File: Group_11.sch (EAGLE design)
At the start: 28 parts, among them J1 POWER_JACKPTH_LOCK, U1 +12v

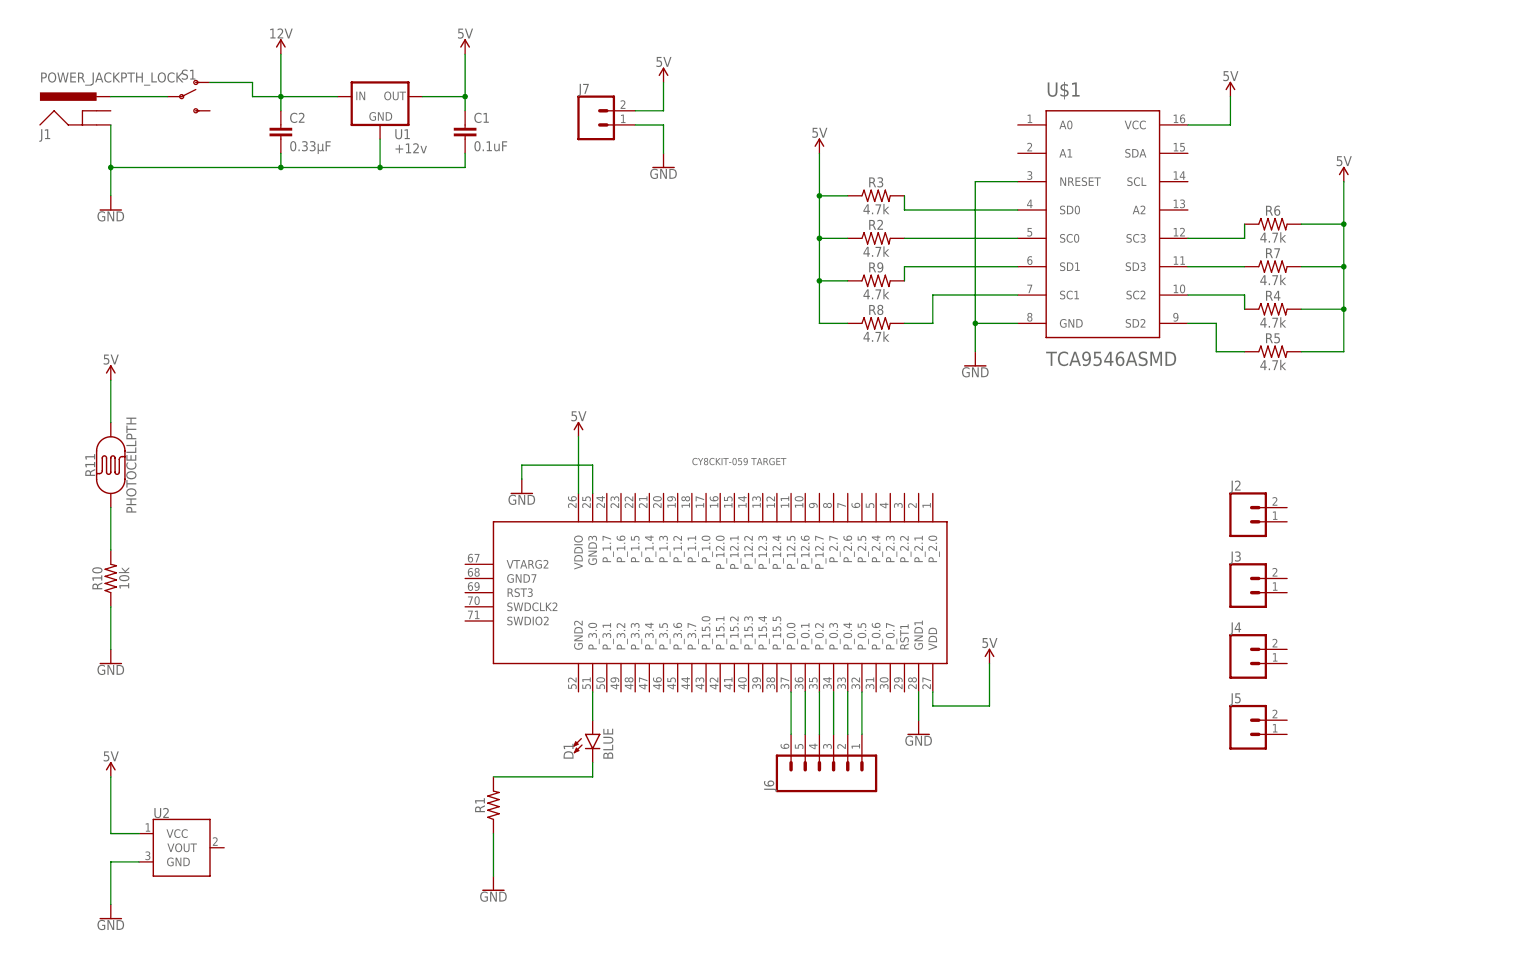
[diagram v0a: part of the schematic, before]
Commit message: Aggiunta dei Labels alla prima versione dello schematico
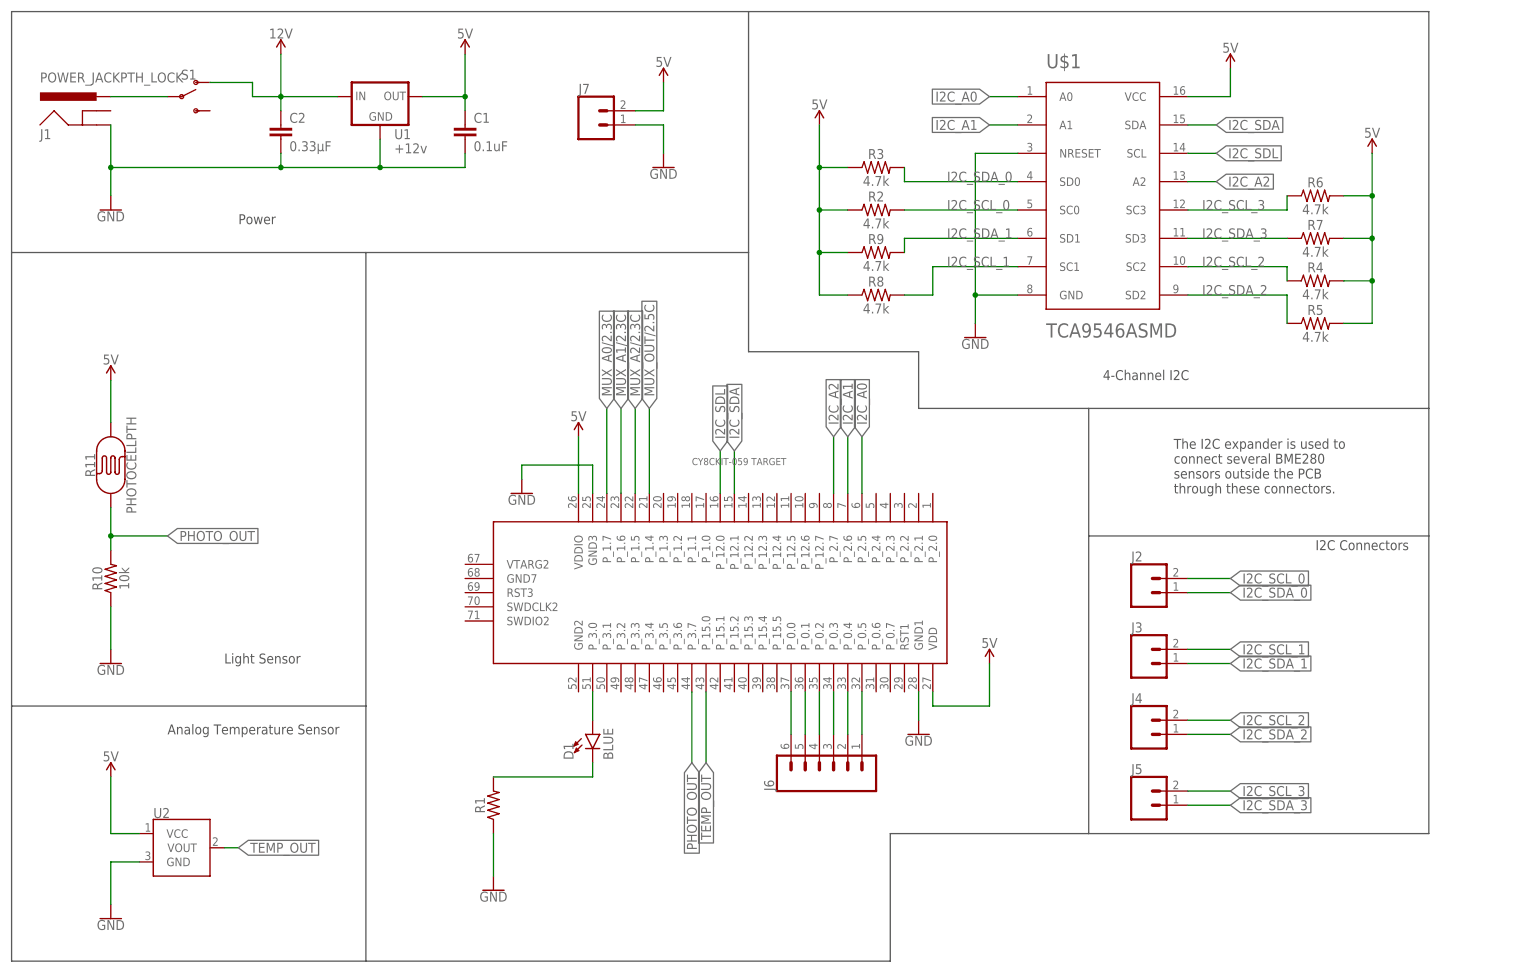
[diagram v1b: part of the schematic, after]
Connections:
- removed net N$1: J6.1, U$2.P_0.5, U$2.P_12.1
- removed net N$10: R3.2, U$1.SD0
- removed net N$11: R2.2, U$1.SC0
- removed net N$12: R6.1, U$1.SC3
- removed net N$13: R7.1, U$1.SD3
- removed net N$14: R4.1, U$1.SC2
- removed net N$15: R5.1, U$1.SD2
- removed net N$16: R9.2, U$1.SD1
- removed net N$17: R8.2, U$1.SC1
- removed net N$18: R10.2, R11.P$1
- new net I2C_A0: U$1.A0, U$2.P_2.5
- new net I2C_A1: U$1.A1, U$2.P_2.6
- new net I2C_A2: U$1.A2, U$2.P_2.7
- new net I2C_SCL_0: J2.2, R2.2, U$1.SC0
- new net I2C_SCL_1: J3.2, R8.2, U$1.SC1
- new net I2C_SCL_2: J4.2, R4.1, U$1.SC2
- new net I2C_SCL_3: J5.2, R6.1, U$1.SC3
- new net I2C_SDA: J6.1, U$1.SDA, U$2.P_0.5, U$2.P_12.1
- new net I2C_SDA_0: J2.1, R3.2, U$1.SD0
- new net I2C_SDA_1: J3.1, R9.2, U$1.SD1
- new net I2C_SDA_2: J4.1, R5.1, U$1.SD2
- new net I2C_SDA_3: J5.1, R7.1, U$1.SD3
- new net I2C_SDL: U$1.SCL, U$2.P_12.0
- new net MUX_A0/2.3C: U$2.P_1.7
- new net MUX_A1/2.3C: U$2.P_1.6
- new net MUX_A2/2.3C: U$2.P_1.5
- new net MUX_OUT/2.5C: U$2.P_1.4
- new net PHOTO_OUT: R10.2, R11.P$1, U$2.P_3.7
- new net TEMP_OUT: U$2.P_15.0, U2.VOUT
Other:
- note added: "4-Channel I2C"
- note added: "Analog Temperature Sensor"
- note added: "I2C Connectors"
- note added: "Light Sensor"
- note added: "Power"
- note added: "The I2C expander is used to connect several BME280 sensors outside the PCB through these connectors."
- moved on the sheet: J2, J3, J4, J5, R2, R3, R4, R5, R6, R7, R8, R9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
